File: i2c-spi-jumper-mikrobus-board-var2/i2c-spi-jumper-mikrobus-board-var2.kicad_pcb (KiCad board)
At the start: 2 copper layers, 25.4 x 28.6 mm, 10 parts, among them J1 mikroBUS_L, J2 mikroBUS_R, U1 SC18IS606PW

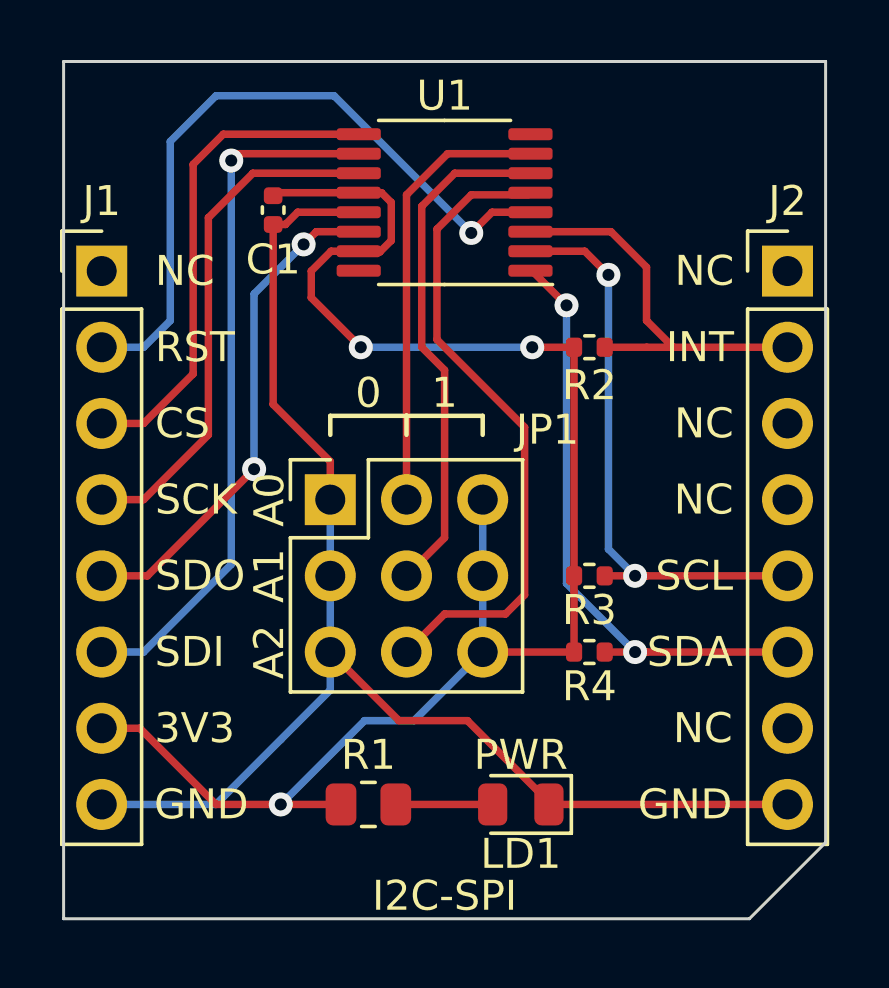
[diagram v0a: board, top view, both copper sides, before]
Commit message: i2c-spi-jumper-var2: add JLCPCB mounting holes
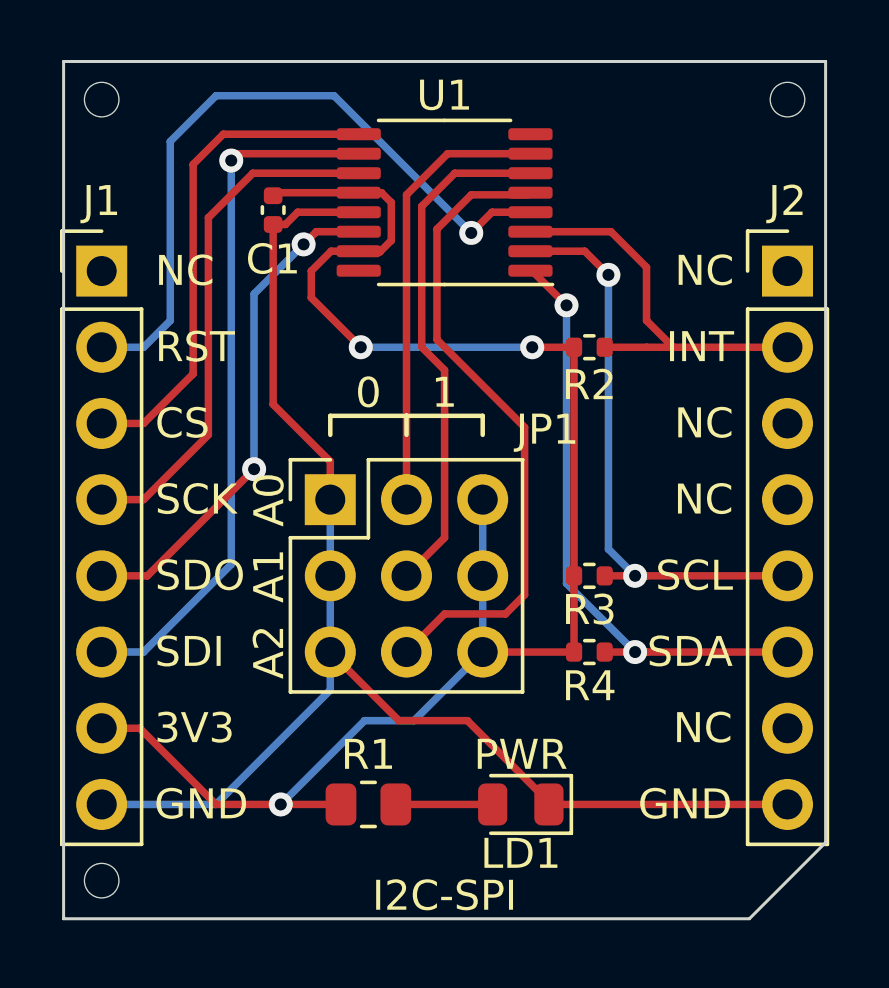
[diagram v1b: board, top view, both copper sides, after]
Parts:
- added REF**: JLCPCB_Mounting_Hole, JLCPCB:JLCPCB_Mounting_Hole, F.Cu at (26.7, 23.5)
- added REF**: JLCPCB_Mounting_Hole, JLCPCB:JLCPCB_Mounting_Hole, F.Cu at (26.7, 49.5)
- added REF**: JLCPCB_Mounting_Hole, JLCPCB:JLCPCB_Mounting_Hole, F.Cu at (49.5, 23.5)
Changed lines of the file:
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@@
     )
+  )
+  (footprint "JLCPCB:JLCPCB_Mounting_Hole" (layer "F.Cu")
+    (at 26.67 23.495)
+    (attr board_only exclude_from_pos_files exclude_from_bom)
+    (fp_text reference "REF**" (at 0 -0.5 unlocked) (layer "F.SilkS") hide
+      (effects (font (size 1 1) (thickness 0.15)))
+    )
+    (fp_text value "JLCPCB_Mounting_Hole" (at 0 1.524 unlocked) (layer "F.Fab")
+      (effects (font (size 1 1) (thickness 0.15)))
+    )
+    (fp_text user "${REFERENCE}" (at 0 2.5 unlocked) (layer "F.Fab") hide
+      (effects (font (size 1 1) (thickness 0.15)))
+    )
+    (pad "" np_thru_hole circle (at 0 0) (size 1.152 1.152) (drill 1.152) (layers F&B.Cu *.Mask)
+      (solder_mask_margin 0.148))
   )
   (footprint "Resistor_SMD:R_0402_1005Metric" (layer "F.Cu")
@@
       (rotate (xyz 0 0 0))
     )
+  )
+  (footprint "JLCPCB:JLCPCB_Mounting_Hole" (layer "F.Cu")
+    (at 26.67 49.53)
+    (attr board_only exclude_from_pos_files exclude_from_bom)
+    (fp_text reference "REF**" (at 0 -0.5 unlocked) (layer "F.SilkS") hide
+      (effects (font (size 1 1) (thickness 0.15)))
+    )
+    (fp_text value "JLCPCB_Mounting_Hole" (at 0 1.524 unlocked) (layer "F.Fab")
+      (effects (font (size 1 1) (thickness 0.15)))
+    )
+    (fp_text user "${REFERENCE}" (at 0 2.5 unlocked) (layer "F.Fab") hide
+      (effects (font (size 1 1) (thickness 0.15)))
+    )
+    (pad "" np_thru_hole circle (at 0 0) (size 1.152 1.152) (drill 1.152) (layers F&B.Cu *.Mask)
+      (solder_mask_margin 0.148))
   )
   (footprint "Resistor_SMD:R_0402_1005Metric" (layer "F.Cu")
@@
     )
   )
+  (footprint "JLCPCB:JLCPCB_Mounting_Hole" (layer "F.Cu")
+    (at 49.53 23.495)
+    (attr board_only exclude_from_pos_files exclude_from_bom)
+    (fp_text reference "REF**" (at 0 -0.5 unlocked) (layer "F.SilkS") hide
+      (effects (font (size 1 1) (thickness 0.15)))
+    )
+    (fp_text value "JLCPCB_Mounting_Hole" (at 0 1.524 unlocked) (layer "F.Fab")
+      (effects (font (size 1 1) (thickness 0.15)))
+    )
+    (fp_text user "${REFERENCE}" (at 0 2.5 unlocked) (layer "F.Fab") hide
+      (effects (font (size 1 1) (thickness 0.15)))
+    )
+    (pad "" np_thru_hole circle (at 0 0) (size 1.152 1.152) (drill 1.152) (layers F&B.Cu *.Mask)
+      (solder_mask_margin 0.148))
+  )
   (gr_line (start 36.83 34.671) (end 36.83 34.036) (layer "F.SilkS") (width 0.15))

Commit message: i2c-spi-jumper-var2: add jumper to enable/disable ~INT pin connection
This allows mikroBUS boards like the OLED C click to be used with this
board without causing their Enable pin, which shares its location with the
~Interrupt pin, to be pulled low after SPI communication completes.
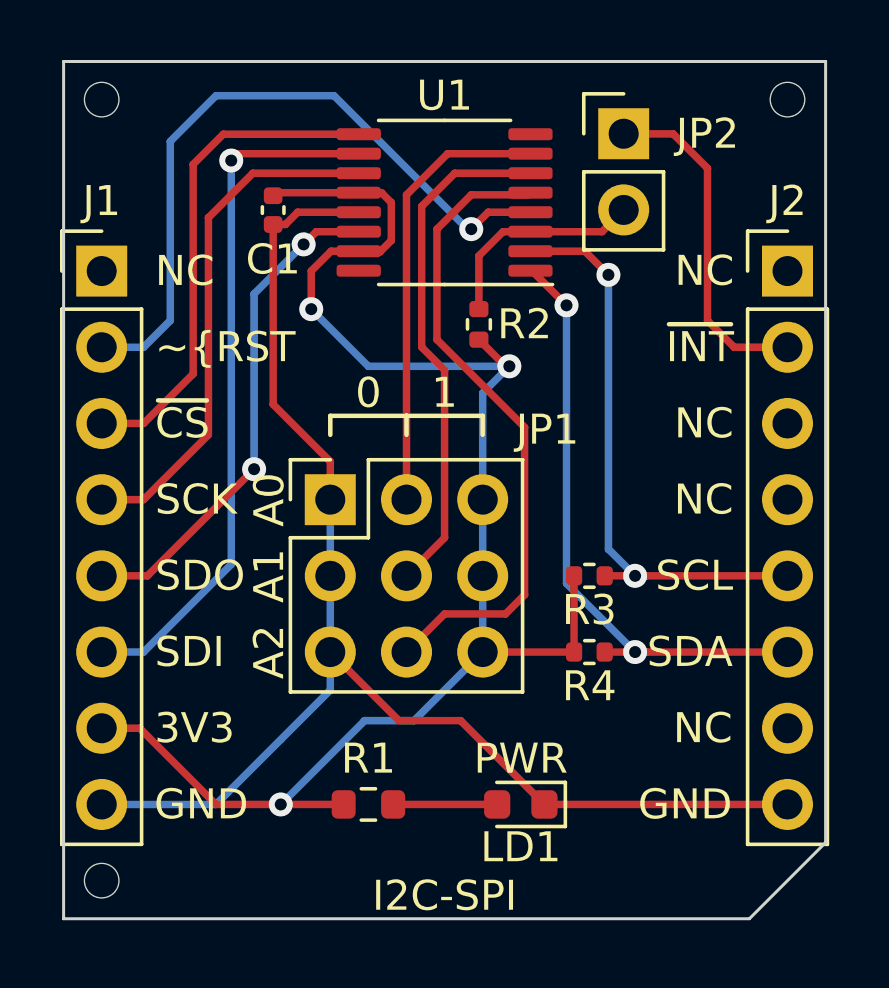
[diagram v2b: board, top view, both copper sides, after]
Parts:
- added JP2: INT_Jumper, Connector_PinHeader_2.54mm:PinHeader_1x02_P2.54mm_Vertical, F.Cu at (44.1, 24.6)
- LD1: footprint LED_SMD:LED_0805_2012Metric -> LED_SMD:LED_0603_1608Metric
- R1: footprint Resistor_SMD:R_0805_2012Metric -> Resistor_SMD:R_0603_1608Metric
- moved R2 3.76 mm to (39.2, 31.0), turned to 90 degrees
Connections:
- net /CS renamed /~{CS}
- net /RST renamed /~{RST}
- J2 pad 2: /INT -> Net-(J2-Pad2)
- R2 pad 2: /INT -> /~{INT}
- U1 pad 3: /INT -> /~{INT}
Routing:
- net /INT: track 13.5 -> 0.00 mm
- net Net-(J2-Pad2): track 0.00 -> 11.4 mm
- net /~{INT}: track 0.00 -> 7.24 mm
- net /3V3: track 54.9 -> 51.8 mm
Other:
- board text added: "~{CS}"
- board text added: "~{INT}"
- board text added: "~{RST"
- board text removed: "CS"
- board text removed: "INT"
- board text removed: "RST"
